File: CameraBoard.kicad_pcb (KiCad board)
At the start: 2 copper layers, 61 x 100 mm, 32 parts, among them J1 BNC_75_OHM_HORIZ, J2 BNC_75_OHM_HORIZ, U1 TM4C129E_Launchpad, U2 AP1509-33SG-13, U3 MAX4314ESD+, U4 MAX4314ESD+

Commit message: Minor routing clean up
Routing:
- net +3.3V: track 94.5 -> 99.8 mm
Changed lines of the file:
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@@
     (thickness 1.6)
     (drawings 19)
-    (tracks 237)
+    (tracks 240)
     (zones 0)
     (modules 32)
@@
   )
   (setup
-    (last_trace_width 0.254)
+    (last_trace_width 0.25)
     (user_trace_width 0.254)
     (user_trace_width 0.8128)
@@
   (segment (start 129.3114 93.6244) (end 129.3114 99.4918) (width 0.254) (layer B.Cu) (net 3))
   (via (at 111.0488 117.348) (size 0.8) (drill 0.4) (layers F.Cu B.Cu) (net 3))
-  (segment (start 129.3114 99.4918) (end 111.4552 117.348) (width 0.254) (layer B.Cu) (net 3))
-  (segment (start 111.4552 117.348) (end 111.0488 117.348) (width 0.254) (layer B.Cu) (net 3))
   (segment (start 111.0488 117.348) (end 108.6028 117.348) (width 0.254) (layer F.Cu) (net 3))
+  (segment (start 129.3114 99.4918) (end 127.381 101.4222) (width 0.25) (layer B.Cu) (net 3))
+  (segment (start 127.381 101.4222) (end 127.381 110.49) (width 0.25) (layer B.Cu) (net 3))
+  (segment (start 127.381 110.49) (end 125.349 112.522) (width 0.25) (layer B.Cu) (net 3))
+  (segment (start 115.8748 112.522) (end 111.0488 117.348) (width 0.25) (layer B.Cu) (net 3))
+  (segment (start 125.349 112.522) (end 115.8748 112.522) (width 0.25) (layer B.Cu) (net 3))
   (segment (start 135.8724 97.2644) (end 136.1186 97.5106) (width 0.254) (layer F.Cu) (net 4))
   (segment (start 132.1308 97.2644) (end 135.8724 97.2644) (width 0.254) (layer F.Cu) (net 4))

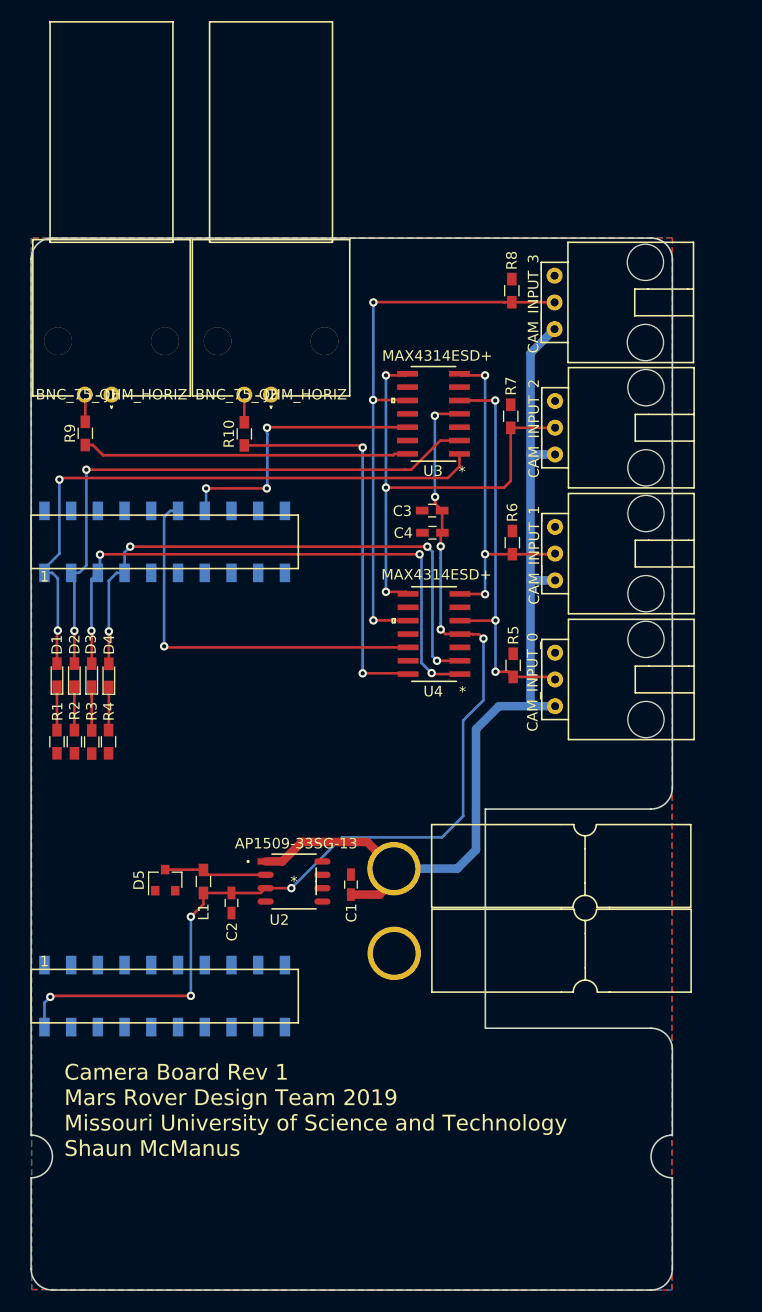
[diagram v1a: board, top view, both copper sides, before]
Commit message: Completed schematic changes from PDR, currently partway through layout changes. Uploading progress, details listed in the PDR Notes documentation with marks for each item completed
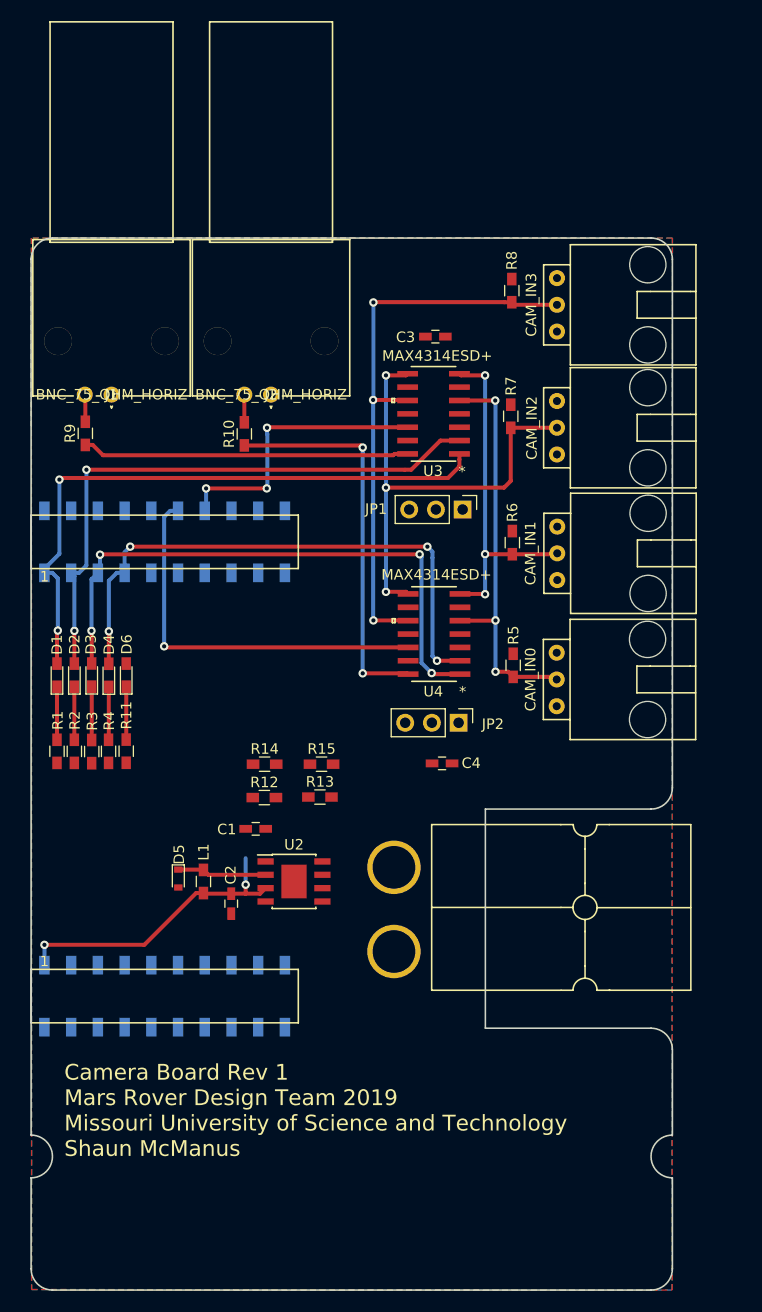
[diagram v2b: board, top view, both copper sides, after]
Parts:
- removed CAM_INPUT_0: CAM_0, MRDT_Connectors:MOLEX_SL_03_Horizontal
- removed CAM_INPUT_1: CAM_1, MRDT_Connectors:MOLEX_SL_03_Horizontal
- removed CAM_INPUT_2: CAM_2, MRDT_Connectors:MOLEX_SL_03_Horizontal
- removed CAM_INPUT_3: CAM_3, MRDT_Connectors:MOLEX_SL_03_Horizontal
- removed Conn2: AndersonPP_GND, MRDT_Connectors:Anderson_1_Horisontal
- added CAM_IN0: CAM_0, MRDT_Connectors:MOLEX_SL_03_Horizontal, F.Cu at (136.3, 97.5)
- added CAM_IN1: CAM_1, MRDT_Connectors:MOLEX_SL_03_Horizontal, F.Cu at (136.3, 85.5)
- added CAM_IN2: CAM_2, MRDT_Connectors:MOLEX_SL_03_Horizontal, F.Cu at (136.3, 73.6)
- added CAM_IN3: CAM_3, MRDT_Connectors:MOLEX_SL_03_Horizontal, F.Cu at (136.3, 61.9)
- added D6: LED, LEDs:LED_0603_HandSoldering, F.Cu at (95.4, 97.1)
- added JP1: Jumper_NC_Dual, Pin_Headers:Pin_Header_Straight_1x03_Pitch2.54mm, F.Cu at (127.3, 81.4)
- added JP2: Jumper_NC_Dual, Pin_Headers:Pin_Header_Straight_1x03_Pitch2.54mm, F.Cu at (126.9, 101.6)
- added R11: 500, Resistors_SMD:R_0603_HandSoldering, F.Cu at (95.4, 104.3)
- added R12: 100, Resistors_SMD:R_0603_HandSoldering, F.Cu at (108.5, 108.7)
- added R13: 500, Resistors_SMD:R_0603_HandSoldering, F.Cu at (113.8, 108.7)
- added R14: 100, Resistors_SMD:R_0603_HandSoldering, F.Cu at (108.5, 105.6)
- added R15: 500, Resistors_SMD:R_0603_HandSoldering, F.Cu at (113.9, 105.6)
- C1: value 1u -> 10u
- Conn1: value AndersonPP_LOG -> AndersonPP; footprint MRDT_Connectors:Anderson_1_Horisontal -> MRDT_Connectors:Anderson_2_Horisontal_Side_by_Side
- D5: footprint Diodes_SMD:D_SOT-23_ANK -> Diodes_SMD:D_0603
- U2: value AP1509-33SG-13 -> AP1059; footprint AP150933SG13:AP1509-33SG-13 -> Housings_SOIC:HTSOP-8-1EP_3.9x4.9mm_Pitch1.27mm
- moved C4 21.9 mm to (125.4, 105.5), turned to 0 degrees
- moved C3 16.5 mm to (124.7, 64.9)
- moved C1 10.5 mm to (107.7, 111.7), turned to 180 degrees
- moved D5 1.25 mm to (100.3, 116.4), turned to 270 degrees
- moved R1 0.91 mm to (88.8, 104.3)
- moved R2 0.91 mm to (90.4, 104.3)
- moved R3 0.91 mm to (92.1, 104.4)
- moved R4 0.91 mm to (93.7, 104.3)
- moved C2 0.07 mm to (105.3, 118.8), turned to 90 degrees
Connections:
- C2 pad 1: +3.3V -> GND
- C2 pad 2: GND -> +5V
- C3 pad 1: +3.3V -> Net-(C3-Pad1)
- C4 pad 1: +3.3V -> Net-(C4-Pad1)
- Conn1 pad 1: +12V -> GND
- L1 pad 2: +3.3V -> +5V
- U1 pad +3V3: +3.3V -> Net-(U1-Pad+3V3)
- U1 pad +5V: Net-(U1-Pad+5V) -> +5V
- U1 pad PP2: Net-(U1-PadPP2) -> SW_ERR
- U2 pad 3: +3.3V -> +5V
- U3 pad 4: +3.3V -> Net-(C3-Pad1)
- U4 pad 4: +3.3V -> Net-(C4-Pad1)
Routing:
- net +3.3V: track 99.8 -> 0.00 mm, vias 9 -> 0
- net +12V: track 89.8 -> 1.32 mm
- net +5V: track 0.00 -> 28.6 mm, vias 0 -> 2
- net Net-(D6-Pad1): track 0.00 -> 5.03 mm
- net Net-(D5-Pad1): track 9.75 -> 8.54 mm
- net Net-(D4-Pad1): track 4.12 -> 5.03 mm
- net Net-(D3-Pad1): track 4.16 -> 5.07 mm
- net Net-(D2-Pad1): track 4.12 -> 5.04 mm
- net Net-(D1-Pad1): track 4.12 -> 5.04 mm
